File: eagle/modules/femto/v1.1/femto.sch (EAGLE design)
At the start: 29 parts, among them IC1 MEGA8-AI, J1 RJ12RIGHTANGLE-I2C, J2 RJ12RIGHTANGLE-I2C

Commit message: femto routing
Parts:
- removed DB1, DB2, DC1, DC4: (no value), led:LED3MM
- added LED4, LED5, LED6: LED3MM, lpatiny:LED3MM
- added LED7: (no value), adafruit:LEDCHIP-LED0603
- LED3: value (none) -> LED3MM; device adafruit:LEDCHIP-LED0603 -> lpatiny:LED3MM
- renumbered R1 to R8, R2 to R7, RB1 to R5, RB2 to R4, RC1 to R3, RC6 to R6, RD10 to R2C, RD11 to R1A, RD12 to R1B, RD13 to R1C, RD8 to R2A, RD9 to R2B
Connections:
- net GND: now also LED4.C, LED5.C, LED6.C, LED7.C; no longer DB1.C, DB2.C, DC1.C, DC4.C
- net N$1: now also LED2.CRED; no longer LED1.CRED
- net N$15: now also LED7.A; no longer LED3.A
- net N$16: now also LED3.A; no longer DC1.A
- net N$20: now also LED1.CRED; no longer LED2.CRED
- net N$21: now also LED1.CBLUE; no longer LED2.CBLUE
- net N$22: now also LED1.CGREEN; no longer LED2.CGREEN
- net N$23: now also LED6.A; no longer DC4.A
- net N$40: now also LED5.A; no longer DB1.A
- net N$41: now also LED4.A; no longer DB2.A
- net N$7: now also LED2.CBLUE; no longer LED1.CBLUE
- net N$8: now also LED2.CGREEN; no longer LED1.CGREEN
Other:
- moved on the sheet: LED1, LED2, LED3

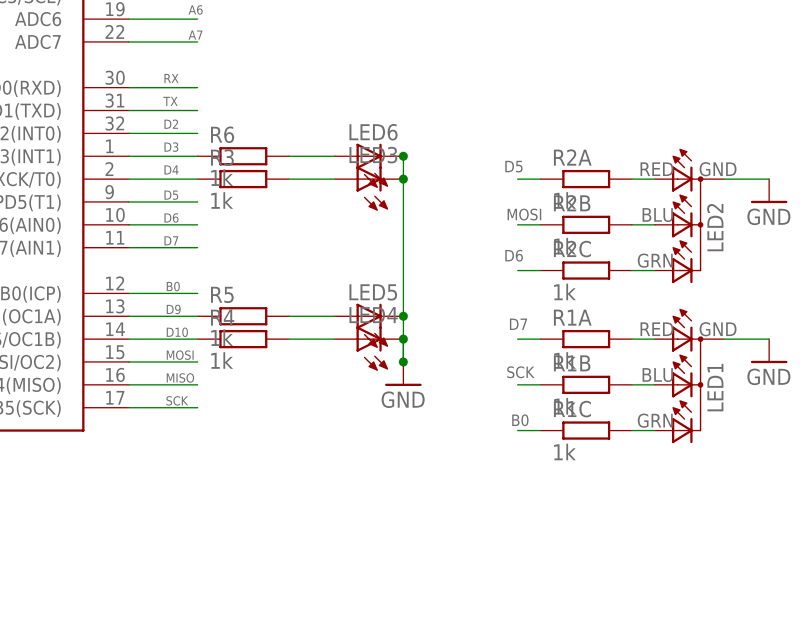
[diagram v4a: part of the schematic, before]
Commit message: Update arduino for soft pwm and 8 mhz
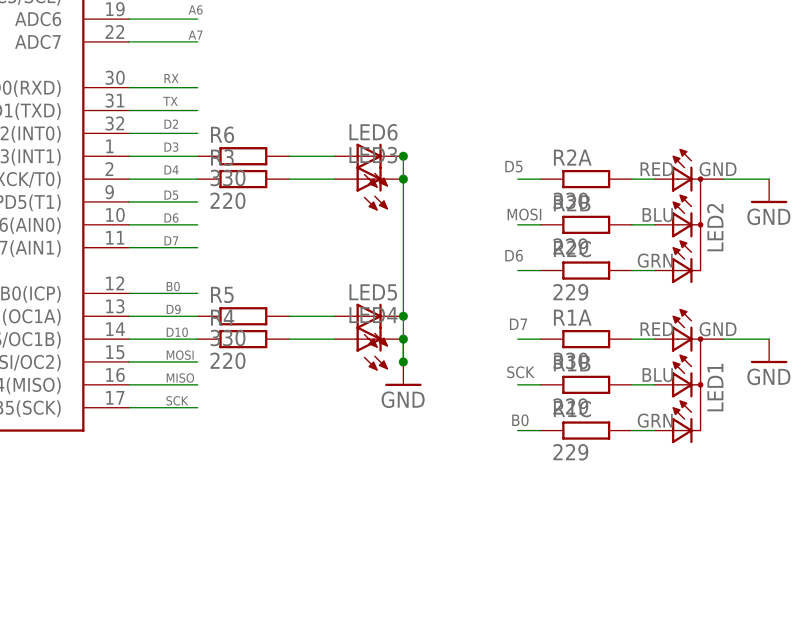
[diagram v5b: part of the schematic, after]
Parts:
- R1A, R2A, R5, R6: value 1k -> 330
- R1B, R1C, R2B, R2C: value 1k -> 229
- R3, R4: value 1k -> 220
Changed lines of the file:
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@@
 <parts>
 <part name="IC1" library="atmel" deviceset="MEGA8" device="-AI"/>
-<part name="R5" library="resistor" deviceset="R-EU_" device="M1206" value="1k"/>
-<part name="R4" library="resistor" deviceset="R-EU_" device="M1206" value="1k"/>
+<part name="R5" library="resistor" deviceset="R-EU_" device="M1206" value="330"/>
+<part name="R4" library="resistor" deviceset="R-EU_" device="M1206" value="220"/>
 <part name="LED5" library="lpatiny" deviceset="LED3MM" device=""/>
 <part name="LED4" library="lpatiny" deviceset="LED3MM" device=""/>
@@
 <part name="LED2" library="lpatiny" deviceset="RGB-COMMON-CATHODE" device=""/>
 <part name="LED1" library="lpatiny" deviceset="RGB-COMMON-CATHODE" device=""/>
-<part name="R2A" library="resistor" deviceset="R-EU_" device="M1206" value="1k"/>
-<part name="R2B" library="resistor" deviceset="R-EU_" device="M1206" value="1k"/>
-<part name="R2C" library="resistor" deviceset="R-EU_" device="M1206" value="1k"/>
-<part name="R1A" library="resistor" deviceset="R-EU_" device="M1206" value="1k"/>
-<part name="R1B" library="resistor" deviceset="R-EU_" device="M1206" value="1k"/>
-<part name="R1C" library="resistor" deviceset="R-EU_" device="M1206" value="1k"/>
+<part name="R2A" library="resistor" deviceset="R-EU_" device="M1206" value="330"/>
+<part name="R2B" library="resistor" deviceset="R-EU_" device="M1206" value="229"/>
+<part name="R2C" library="resistor" deviceset="R-EU_" device="M1206" value="229"/>
+<part name="R1A" library="resistor" deviceset="R-EU_" device="M1206" value="330"/>
+<part name="R1B" library="resistor" deviceset="R-EU_" device="M1206" value="229"/>
+<part name="R1C" library="resistor" deviceset="R-EU_" device="M1206" value="229"/>
 <part name="GND7" library="supply1" deviceset="GND" device=""/>
 <part name="GND8" library="supply1" deviceset="GND" device=""/>
 <part name="GND3" library="supply1" deviceset="GND" device=""/>
-<part name="R6" library="resistor" deviceset="R-EU_" device="M1206" value="1k"/>
+<part name="R6" library="resistor" deviceset="R-EU_" device="M1206" value="330"/>
 <part name="LED6" library="lpatiny" deviceset="LED3MM" device=""/>
 <part name="GND2" library="supply1" deviceset="GND" device=""/>
@@
 <part name="D2" library="lpatiny" deviceset="1N581*" device="D1206" value="1N581D1206"/>
 <part name="P+5" library="supply1" deviceset="+5V" device=""/>
-<part name="R3" library="resistor" deviceset="R-EU_" device="M1206" value="1k"/>
+<part name="R3" library="resistor" deviceset="R-EU_" device="M1206" value="220"/>
 <part name="LED3" library="lpatiny" deviceset="LED3MM" device=""/>
 </parts>
